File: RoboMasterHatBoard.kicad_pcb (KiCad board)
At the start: 2 copper layers, 48.3 x 38.1 mm, 21 parts, among them J1 Conn_01x08_Socket, J10 Conn_01x02_Pin, J11 Conn_01x03_Pin, J12 Conn_01x05_Pin, J13 Conn_01x05_Pin, J14 Conn_01x03_Pin, J15 Conn_01x03_Pin, J2 Conn_01x08_Socket, J3 Conn_01x08_Socket, J4 Conn_01x08_Socket, J5 Conn_01x08_Socket, J6 Conn_01x08_Socket, J7 Conn_01x10_Socket, J8 Conn_01x10_Socket, J9 Conn_01x02_Pin, U1 AMS1117-3.3

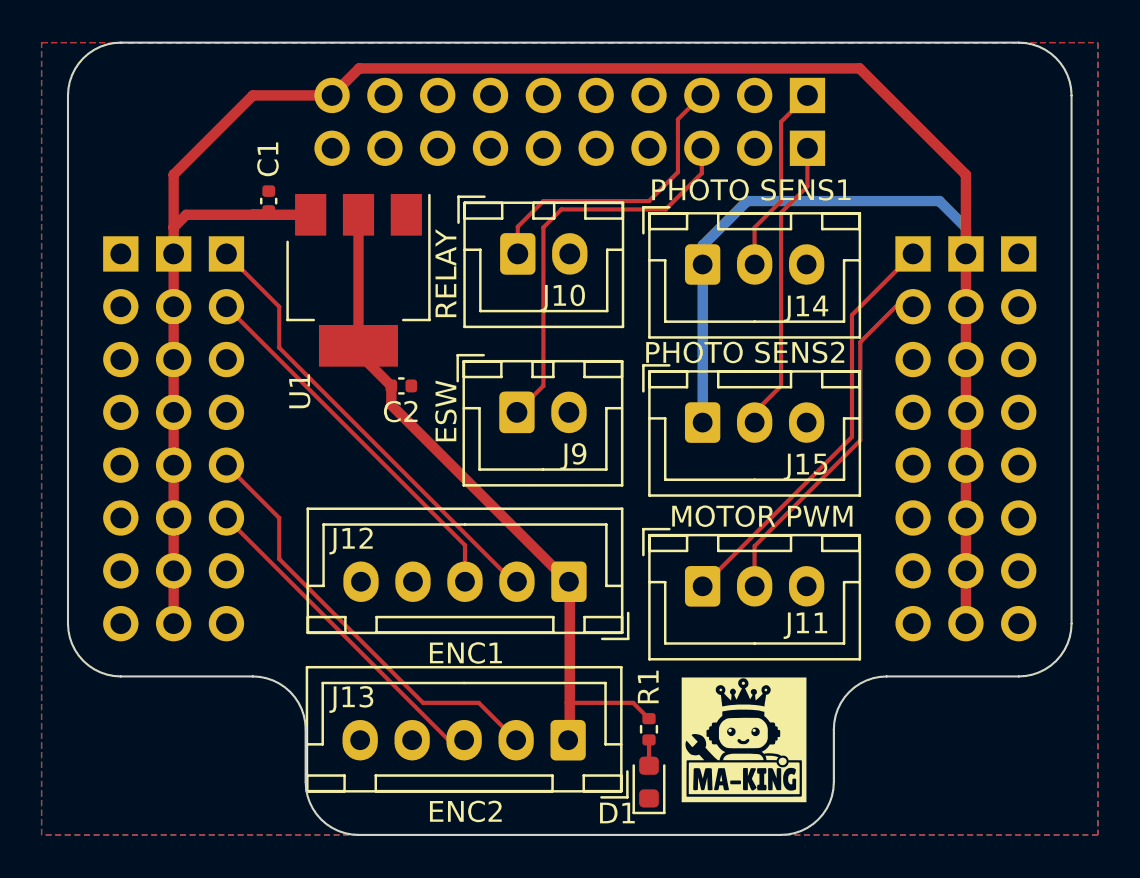
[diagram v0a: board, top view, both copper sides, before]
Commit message: 撃破入力ピンを追加
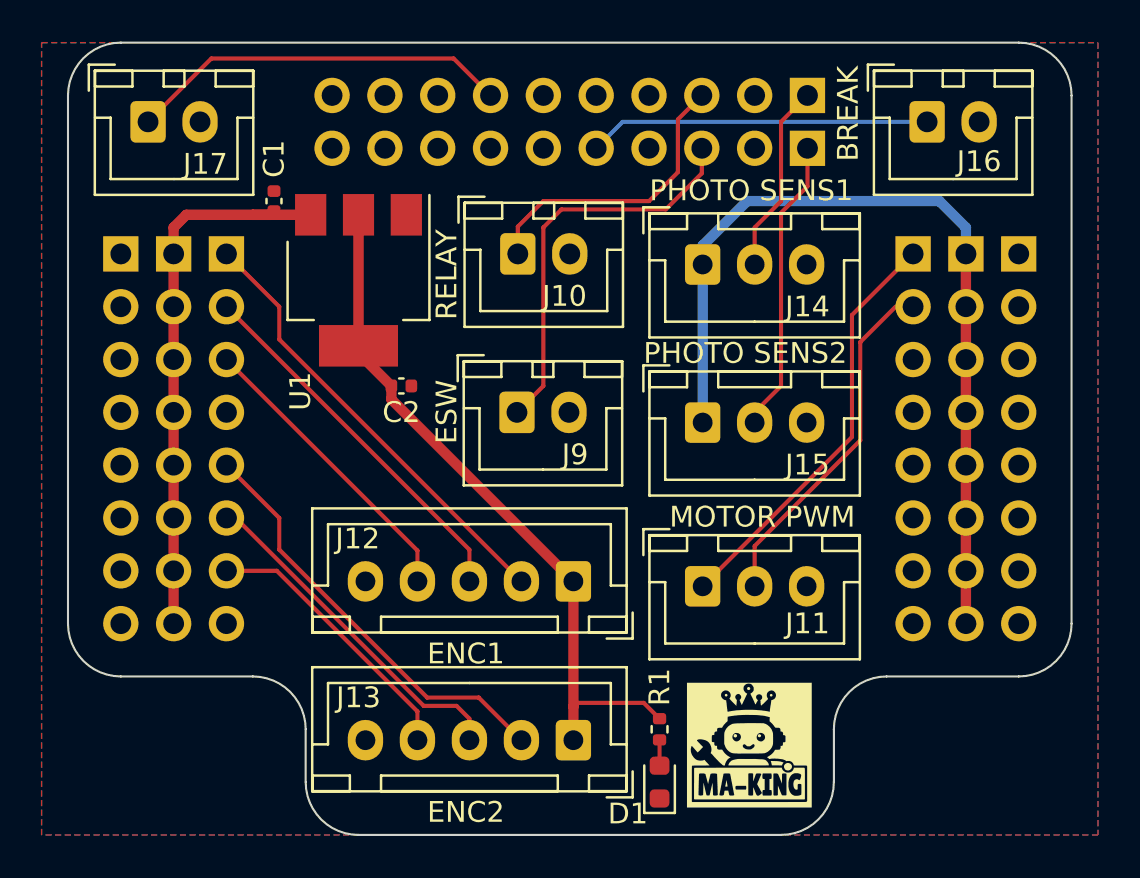
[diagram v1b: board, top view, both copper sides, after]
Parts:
- added J16: Conn_01x02_Pin, Connector_JST:JST_XH_B2B-XH-A_1x02_P2.50mm_Vertical, F.Cu at (130.2, 67.3)
- added J17: Conn_01x02_Pin, Connector_JST:JST_XH_B2B-XH-A_1x02_P2.50mm_Vertical, F.Cu at (92.8, 67.3)
- moved D1 0.51 mm to (117.3, 99.1)
- moved R1 0.51 mm to (117.3, 96.5)
- moved   0.36 mm to (121.7, 97.3)
- moved C1 0.25 mm to (98.8, 71.1)
- moved J13 0.25 mm to (113.2, 97.0)
- moved J12 0.21 mm to (113.2, 89.4)
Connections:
- J12 pad 4: unconnected-(J12-Pin_4-Pad4) -> /ENC1_IN_Z
- J13 pad 4: unconnected-(J13-Pin_4-Pad4) -> /ENC2_IN_Z
- J14 pad 1: +5V -> +5C
- J15 pad 1: +5V -> +5C
- J2 pad 1: +5V -> +5C
- J2 pad 2: +5V -> +5C
- J2 pad 3: +5V -> +5C
- J2 pad 4: +5V -> +5C
- J2 pad 5: +5V -> +5C
- J2 pad 6: +5V -> +5C
- J2 pad 7: +5V -> +5C
- J2 pad 8: +5V -> +5C
- J6 pad 3: unconnected-(J6-Pin_3-Pad3) -> /ENC1_IN_Z
- J6 pad 7: unconnected-(J6-Pin_7-Pad7) -> /ENC2_IN_Z
- J7 pad 5: unconnected-(J7-Pin_5-Pad5) -> /BRAKE_INPUT
- J8 pad 10: +5V -> +5F
- J8 pad 7: unconnected-(J8-Pin_7-Pad7) -> /IO1
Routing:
- net +5V: track 117.0 -> 27.0 mm
- net +5C: track 0.00 -> 41.6 mm
- net /IO1: track 0.00 -> 18.5 mm
- net /BRAKE_INPUT: track 0.00 -> 16.4 mm
- net /ENC1_IN_Z: track 0.00 -> 14.5 mm
- net /ENC2_IN_Z: track 0.00 -> 13.4 mm
- net /ENC2_IN_TIM8_CH2: track 15.9 -> 16.7 mm
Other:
- board text added: "BREAK"
